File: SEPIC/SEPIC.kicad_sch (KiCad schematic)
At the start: 9 parts, among them Q1 NMOS

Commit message: Placa v0.1
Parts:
- removed L2: 1.93m, symbol Device:L
- removed V1: VPWL, symbol Simulation_SPICE:VPWL
- removed V2: 24, symbol Simulation_SPICE:VDC
- added C4: 0.1u, Capacitor_THT:C_Disc_D3.8mm_W2.6mm_P2.50mm, symbol Device:C
- added J1: Barrel Jack, Connector_BarrelJack:BarrelJack_Horizontal, symbol Connector:Barrel_Jack
- added J2: Pin Header, Connector_PinHeader_2.54mm:PinHeader_1x02_P2.54mm_Horizontal, symbol Connector_Generic:Conn_01x02
- added J3: Screw Terminal, TerminalBlock_Phoenix:TerminalBlock_Phoenix_MKDS-1,5-2-5.08_1x02_P5.08mm_Horizontal, symbol Connector:Screw_Terminal_01x02
- added U1: HCPL-3120, Package_DIP:DIP-8_W7.62mm, symbol Driver_FET:HCPL-3120
- C1: value 4.7u -> 22u; footprint (none) -> Capacitor_THT:C_Radial_D4.0mm_H7.0mm_P1.50mm
- C2: value 1u -> 22u; footprint (none) -> Capacitor_THT:C_Radial_D4.0mm_H7.0mm_P1.50mm
- C3: value 46u -> 220u; footprint (none) -> Capacitor_THT:C_Radial_D10.0mm_H16.0mm_P5.00mm
- D1: value D_Schottky -> SR502; footprint (none) -> Diode_THT:D_A-405_P7.62mm_Horizontal
- L1: value 1.93m -> 3m; footprint (none) -> Inductor_THT:L_CommonMode_Toroid_Vertical_L43.2mm_W22.9mm_Px17.78mm_Py30.48mm_Bourns_8100; symbol Device:L -> Inductor:L_Coupled
- Q1: value NMOS -> IRF520N; footprint (none) -> Package_TO_SOT_THT:TO-3P-3_Vertical
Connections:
- net +24V: now also L1.3, C4.1, J1.1, U1.8 (VCC); no longer L1.1
- net GND: now also L1.4, C4.2, J1.2, J3.2 (Pin_2), U1.5 (VEE)
- net PWM: now also U1.6 (VO)
- net out: now also J3.1 (Pin_1)
- net at C2.2, D1.2 (A): now also L1.2
- net at C2.1, Q1.1 (D): now also L1.1; no longer L1.2
- new net: J2.1 (Pin_1), U1.3 (C)
- new net: J2.2 (Pin_2), U1.2 (A)
- no-connect marks 0 -> 1
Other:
- note added: "Convertidor SEPIC"
- note added: "Driver MOSFET"
- note added: "Entrada alimentación"
- note added: "Salida"
- company: (none) -> Universidad de Concepción
- title: (none) -> Convertidor DC/DC Sepic
- moved on the sheet: C1, C2, C3, D1, Q1

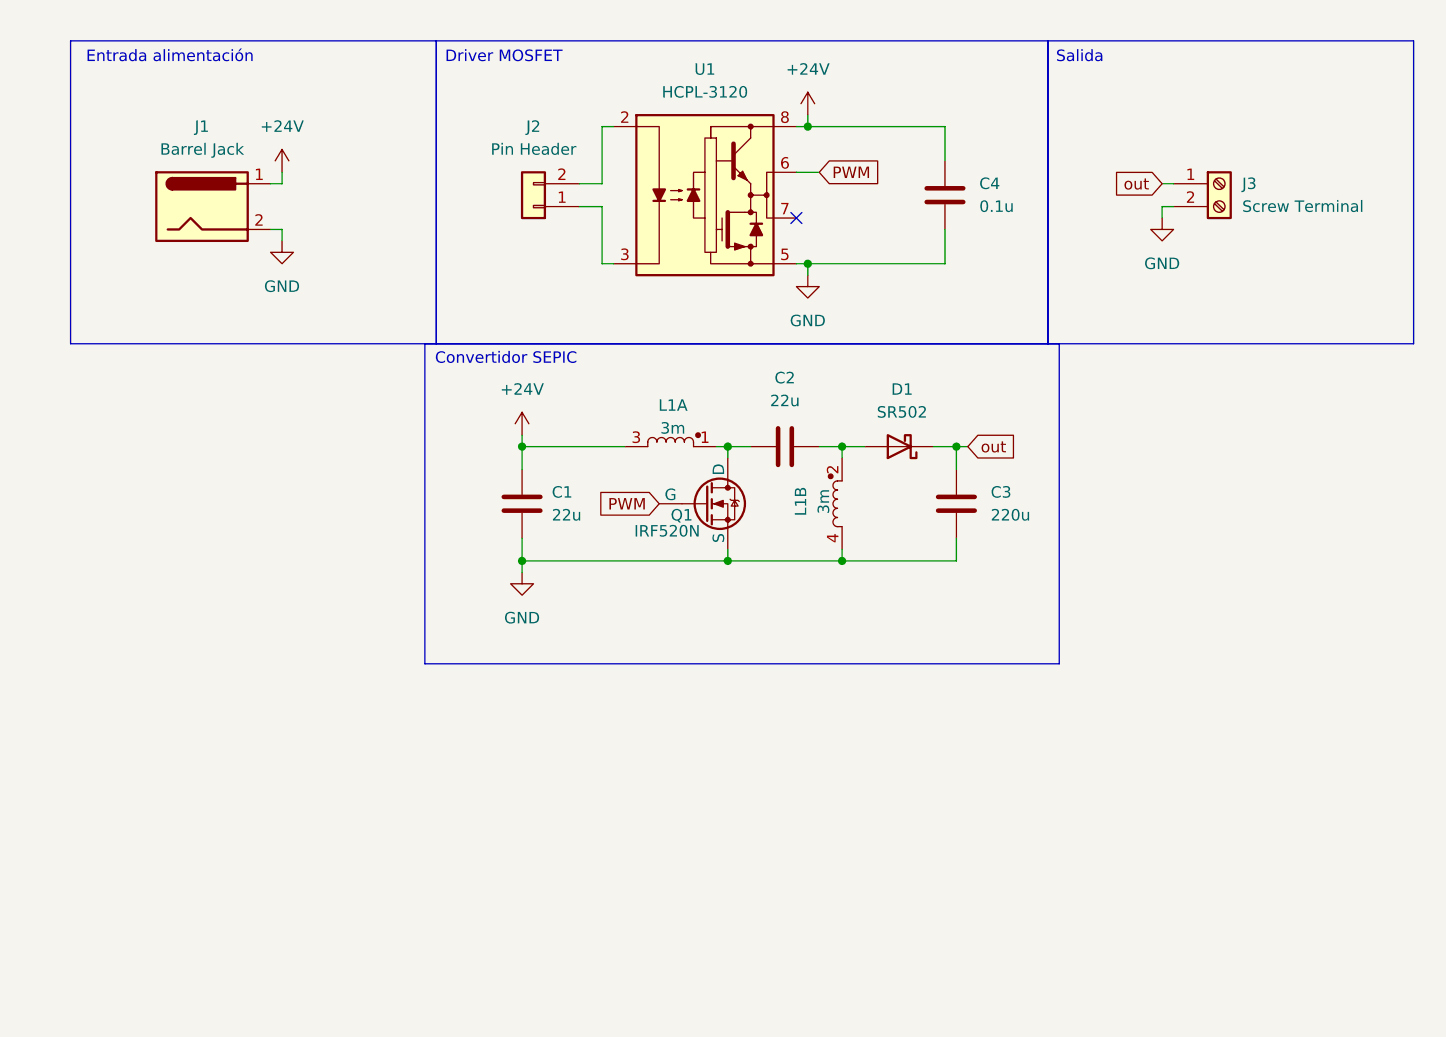
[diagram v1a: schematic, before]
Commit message: Diseño de PCB finalizado, generación de gerber
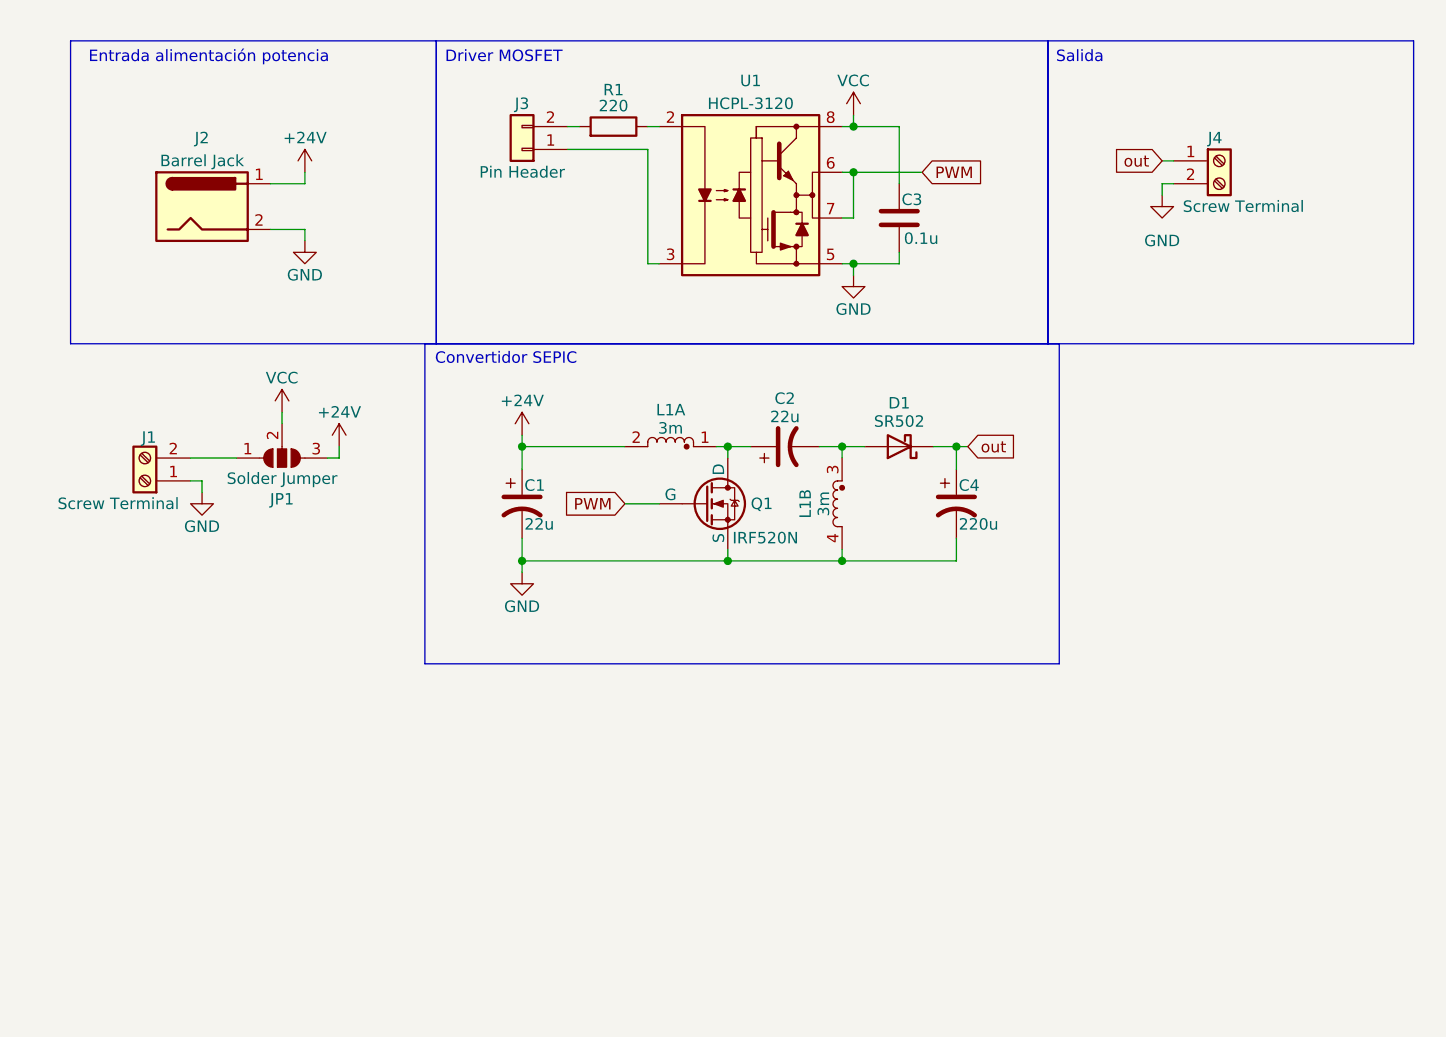
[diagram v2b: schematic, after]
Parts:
- added J1: Screw Terminal, TerminalBlock_Phoenix:TerminalBlock_Phoenix_MKDS-1,5-2-5.08_1x02_P5.08mm_Horizontal, symbol Connector:Screw_Terminal_01x02
- added JP1: Solder Jumper, Jumper:SolderJumper-3_P1.3mm_Open_RoundedPad1.0x1.5mm, symbol Jumper:SolderJumper_3_Open
- added unit 1 of L1
- added R1: 220, Resistor_THT:R_Axial_DIN0309_L9.0mm_D3.2mm_P12.70mm_Horizontal, symbol Device:R
- C1, C2: footprint Capacitor_THT:C_Radial_D4.0mm_H7.0mm_P1.50mm -> Capacitor_THT:C_Radial_D5.0mm_H11.0mm_P2.00mm; symbol Device:C -> Device:C_Polarized_US
- C3: renamed from C4; footprint Capacitor_THT:C_Disc_D3.8mm_W2.6mm_P2.50mm -> Capacitor_THT:C_Disc_D4.7mm_W2.5mm_P5.00mm
- C4: renamed from C3; footprint Capacitor_THT:C_Radial_D10.0mm_H16.0mm_P5.00mm -> Capacitor_THT:C_Radial_D10.0mm_H12.5mm_P5.00mm; symbol Device:C -> Device:C_Polarized_US
- L1: footprint Inductor_THT:L_CommonMode_Toroid_Vertical_L43.2mm_W22.9mm_Px17.78mm_Py30.48mm_Bourns_8100 -> Inductor_THT:L_CommonMode_Toroid_Vertical_L24.0mm_W16.3mm_Px10.16mm_Py20.32mm_Murata_5200
- Q1: footprint Package_TO_SOT_THT:TO-3P-3_Vertical -> Package_TO_SOT_THT:TO-220-3_Vertical
- U1: footprint Package_DIP:DIP-8_W7.62mm -> Package_DIP:DIP-8_W7.62mm_Socket
- renumbered J1 to J2, J2 to J3, J3 to J4
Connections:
- net +24V: now also JP1.3 (B), L1.2; no longer C3.1, L1.3, U1.8 (VCC)
- net GND: now also J1.1 (Pin_1)
- net PWM: now also U1.7 (VO)
- net at J3.2 (Pin_2): now also R1.2; no longer U1.2 (A)
- net at C2.2, D1.2 (A): now also L1.3; no longer L1.2
- net at C2.1, Q1.1 (D): now also L1.1; no longer L1.1
- new net: R1.1, U1.2 (A)
- new net: J1.2 (Pin_2), JP1.1 (A)
- new net VCC: C3.1, JP1.2 (C), U1.8 (VCC)
- no-connect marks 1 -> 0
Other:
- note added: "Entrada alimentación potencia"
- note removed: "Entrada alimentación"
- moved on the sheet: C3, J3, J4, U1

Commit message: Arreglar pines MOSFET
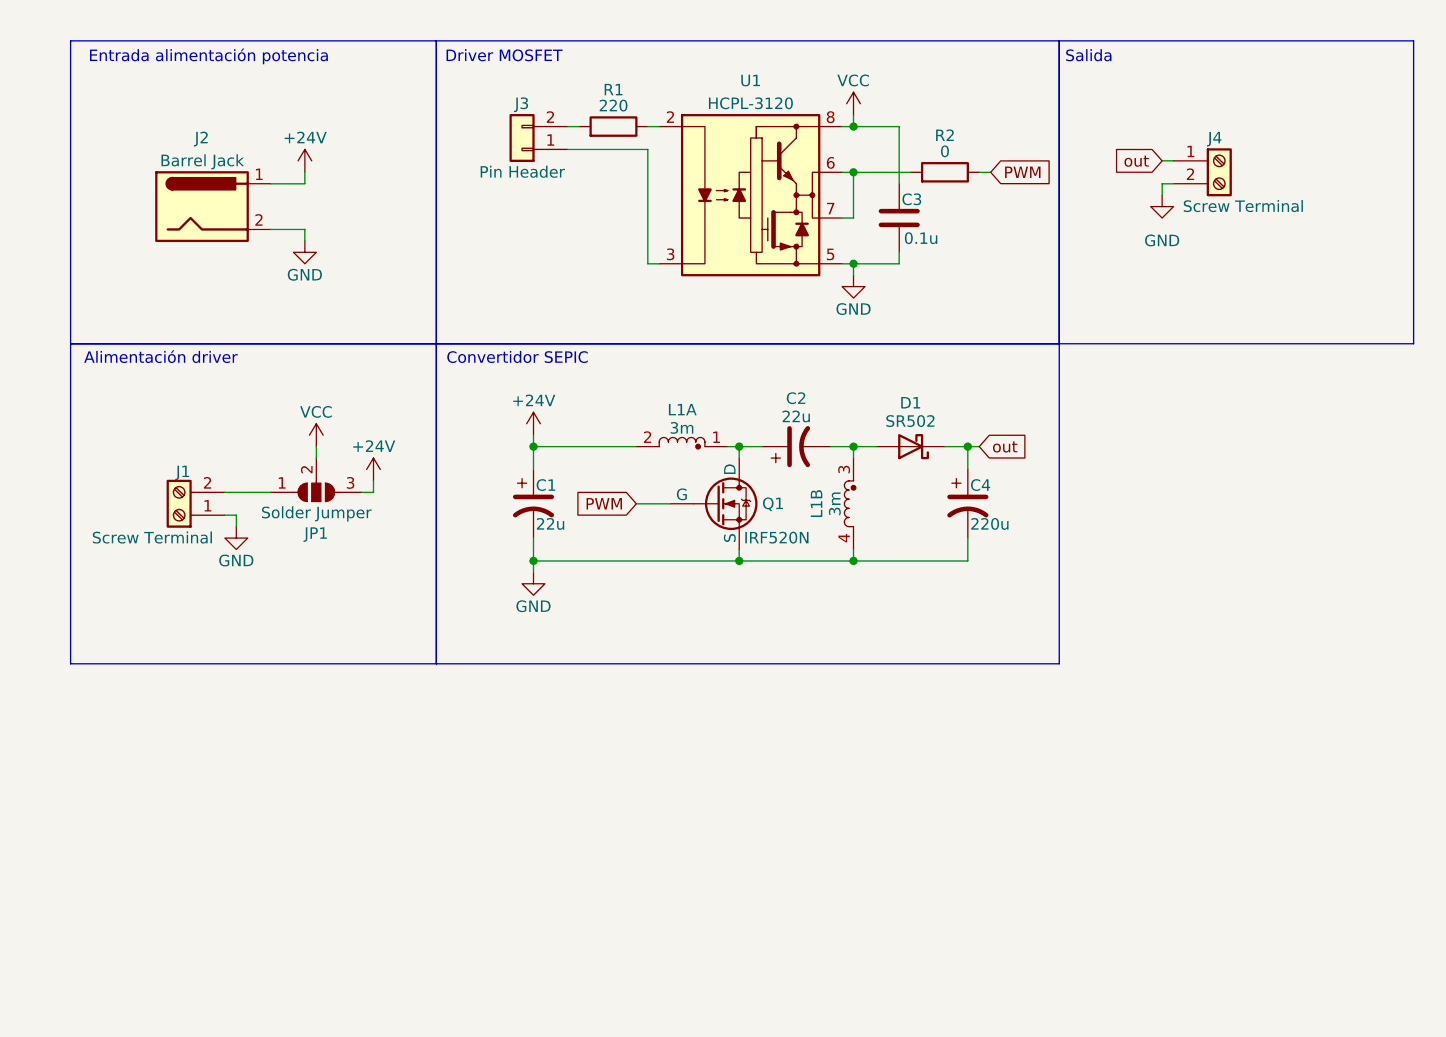
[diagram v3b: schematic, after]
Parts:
- added R2: 0, Resistor_THT:R_Axial_DIN0309_L9.0mm_D3.2mm_P2.54mm_Vertical, symbol Device:R
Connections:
- net PWM: now also Q1.1 (G), R2.1; no longer Q1.2 (G), U1.6 (VO), U1.7 (VO)
- net at C2.1, L1.1: now also Q1.2 (D); no longer Q1.1 (D)
- new net: R2.2, U1.6 (VO), U1.7 (VO)
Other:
- note added: "Alimentación driver"
- moved on the sheet: C1, C2, C4, D1, J1, JP1, L1A, L1B, Q1

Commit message: WIP: redimensionar componentes PCB
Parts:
- C1: footprint Capacitor_THT:C_Radial_D5.0mm_H11.0mm_P2.00mm -> Capacitor_THT:C_Radial_D10.0mm_H20.0mm_P5.00mm
- C2: value 22u -> 2.2u; footprint Capacitor_THT:C_Radial_D5.0mm_H11.0mm_P2.00mm -> Capacitor_THT:C_Rect_L16.5mm_W8.7mm_P15.00mm_MKT; symbol Device:C_Polarized_US -> Device:C
- C4: footprint Capacitor_THT:C_Radial_D10.0mm_H12.5mm_P5.00mm -> Capacitor_THT:C_Radial_D16.0mm_H25.0mm_P7.50mm
- R1: footprint Resistor_THT:R_Axial_DIN0309_L9.0mm_D3.2mm_P12.70mm_Horizontal -> Resistor_THT:R_Axial_DIN0309_L9.0mm_D3.2mm_P2.54mm_Vertical
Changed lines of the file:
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@@
 		(color 0 0 0 0)
+	)
+	(bus_entry
+		(at 107.95 78.74)
+		(size 2.54 2.54)
+		(stroke
+			(width 0)
+			(type default)
+		)
 	)
 	(wire
@@
 			)
 		)
-		(property "Footprint" "Capacitor_THT:C_Radial_D5.0mm_H11.0mm_P2.00mm"
+		(property "Footprint" "Capacitor_THT:C_Radial_D10.0mm_H20.0mm_P5.00mm"
 			(at 77.47 76.2 0)
 			(effects
@@
 			)
 		)
-		(property "Description" "Polarized capacitor, US symbol"
+		(property "Description" "Condensador electrolítico, 22uF 160V"
 			(at 77.47 76.2 0)
 			(effects
@@
 			)
 		)
-		(property "Footprint" "Capacitor_THT:C_Radial_D10.0mm_H12.5mm_P5.00mm"
+		(property "Footprint" "Capacitor_THT:C_Radial_D16.0mm_H25.0mm_P7.50mm"
 			(at 125.73 76.2 0)
 			(effects
@@
 			)
 		)
-		(property "Description" "Polarized capacitor, US symbol"
+		(property "Description" "Condensador electrolítico, 220uF 160v"
 			(at 125.73 76.2 0)
 			(effects
@@
 	)
 	(symbol
-		(lib_id "Device:C_Polarized_US")
+		(lib_id "Device:C")
 		(at 106.68 69.85 90)
 		(unit 1)
@@
 			)
 		)
-		(property "Value" "22u"
+		(property "Value" "2.2u"
 			(at 106.68 66.548 90)
 			(effects
@@
 			)
 		)
-		(property "Footprint" "Capacitor_THT:C_Radial_D5.0mm_H11.0mm_P2.00mm"
-			(at 106.68 69.85 0)
+		(property "Footprint" "Capacitor_THT:C_Rect_L16.5mm_W8.7mm_P15.00mm_MKT"
+			(at 110.49 68.8848 0)
 			(effects
 				(font
@@
 			)
 		)
-		(property "Description" "Polarized capacitor, US symbol"
+		(property "Description" "Condensador cerámico, 2.2uF 250V"
 			(at 106.68 69.85 0)
 			(effects
@@
 			)
 		)
-		(property "Footprint" "Resistor_THT:R_Axial_DIN0309_L9.0mm_D3.2mm_P12.70mm_Horizontal"
+		(property "Footprint" "Resistor_THT:R_Axial_DIN0309_L9.0mm_D3.2mm_P2.54mm_Vertical"
 			(at 86.36 36.068 90)
 			(effects

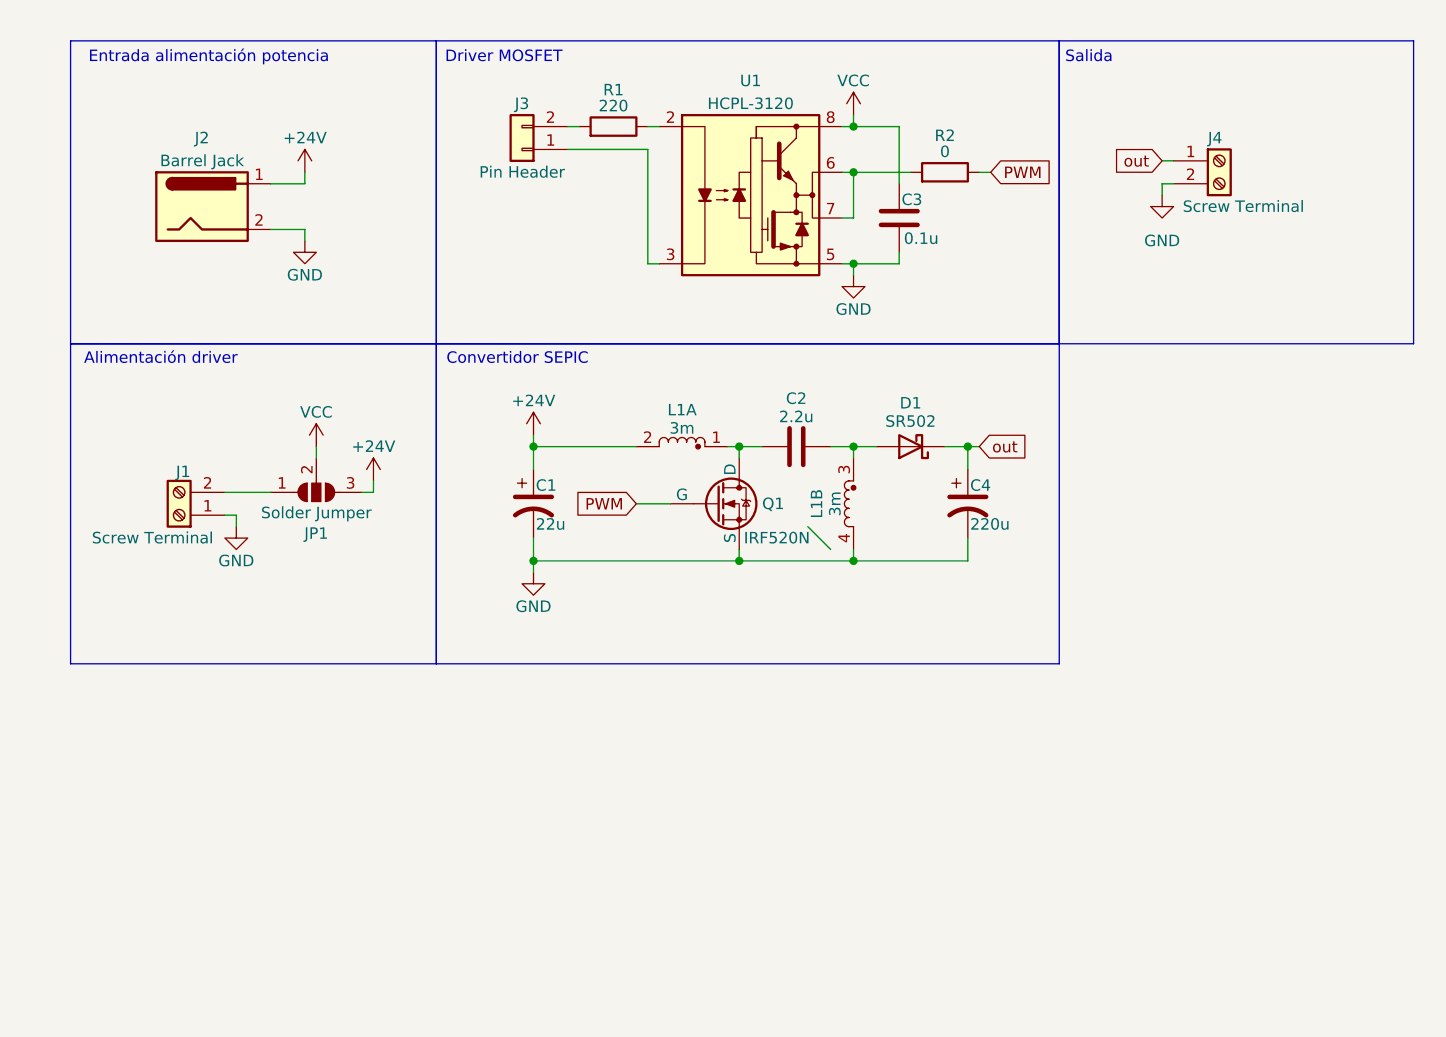
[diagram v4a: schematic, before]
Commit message: Agregar testpoints corriente PCB
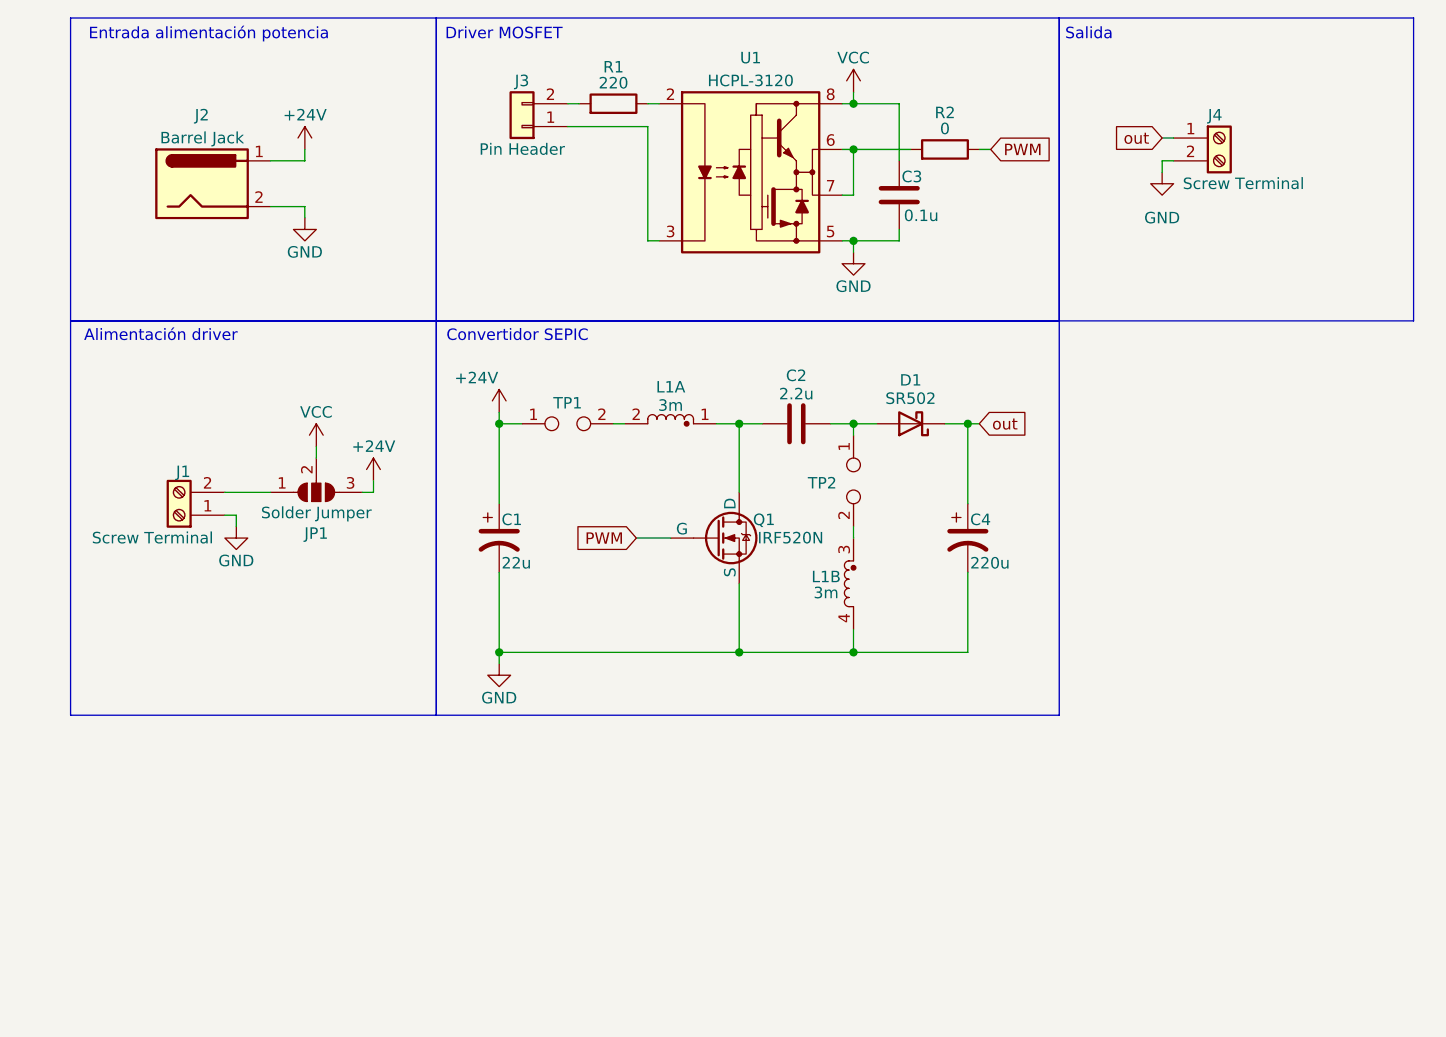
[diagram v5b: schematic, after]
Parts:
- added TP1, TP2: Shunt, TestPoint:TestPoint_2Pads_Pitch5.08mm_Drill1.3mm, symbol Connector:TestPoint_2Pole
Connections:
- net +24V: now also TP1.1; no longer L1.2
- net at C2.2, D1.2 (A): now also TP2.1; no longer L1.3
- new net: L1.3, TP2.2
- new net: L1.2, TP1.2
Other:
- moved on the sheet: C1, C2, C3, C4, D1, J2, J3, J4, L1A, L1B, Q1, R1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
